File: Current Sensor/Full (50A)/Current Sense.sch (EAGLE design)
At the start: 14 parts, among them IC1 INA169

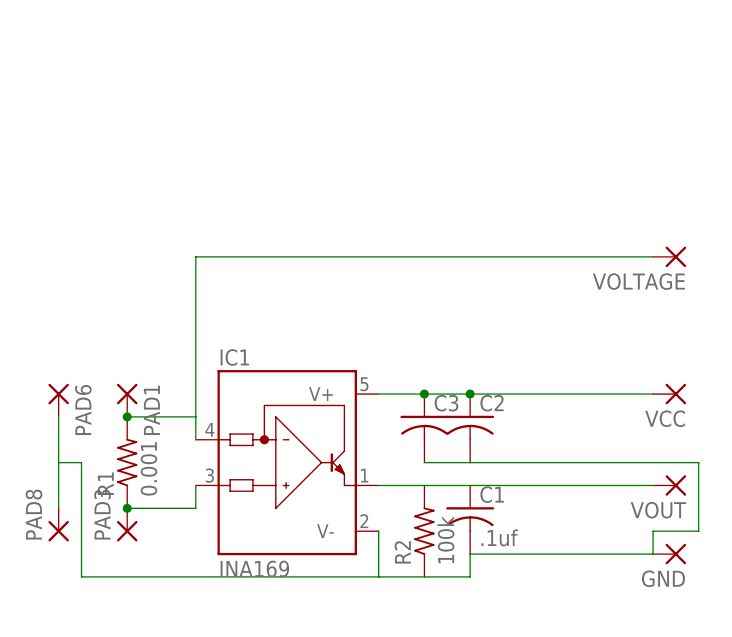
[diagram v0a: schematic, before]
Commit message: Changed Current Sensors
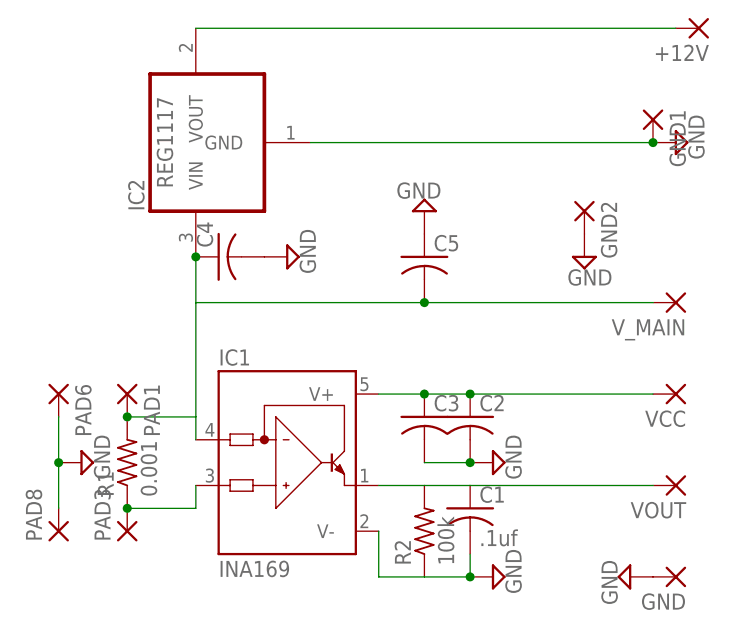
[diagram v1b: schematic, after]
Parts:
- removed VOLTAGE: (no value), wirepad:SMD2
- added +12V, GND1, GND2, V_MAIN: (no value), wirepad:SMD2
- added C4, C5: (no value), adafruit:C-USC0805K
- added IC2: REG1117, burr-brown:REG1117
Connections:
- net N$6 renamed VCC
- removed net N$4: C1.2, C2.2, C3.2, GND.P, IC1.V-, PAD6.P, PAD8.P, R2.1
- new net +12V: +12V.P, IC2.VOUT
- new net GND: C1.2, C2.2, C3.2, C4.2, C5.1, GND.P, GND1.P, GND2.P, IC1.V-, IC2.GND, PAD6.P, PAD8.P, R2.1
- net OUT: now also C4.1, C5.2, IC2.VIN, V_MAIN.P; no longer VOLTAGE.P
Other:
- moved on the sheet: GND
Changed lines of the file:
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@@
 <?xml version="1.0" encoding="utf-8"?>
 <!DOCTYPE eagle SYSTEM "eagle.dtd">
-<eagle version="6.2">
+<eagle version="6.3">
 <drawing>
 <settings>
@@
 <part name="C3" library="adafruit" deviceset="C-US" device="C0805K"/>
 <part name="R1" library="adafruit" deviceset="R-US_" device="R2512" value="0.001"/>
-<part name="VOLTAGE" library="wirepad" deviceset="SMD2" device=""/>
+<part name="V_MAIN" library="wirepad" deviceset="SMD2" device=""/>
+<part name="SUPPLY3" library="supply2" deviceset="GND" device=""/>
+<part name="SUPPLY4" library="supply2" deviceset="GND" device=""/>
+<part name="SUPPLY5" library="supply2" deviceset="GND" device=""/>
+<part name="SUPPLY6" library="supply2" deviceset="GND" device=""/>
+<part name="SUPPLY7" library="supply2" deviceset="GND" device=""/>
+<part name="IC2" library="burr-brown" deviceset="REG1117" device=""/>
+<part name="+12V" library="wirepad" deviceset="SMD2" device=""/>
+<part name="GND1" library="wirepad" deviceset="SMD2" device=""/>
+<part name="GND2" library="wirepad" deviceset="SMD2" device=""/>
+<part name="C4" library="adafruit" deviceset="C-US" device="C0805K"/>
+<part name="C5" library="adafruit" deviceset="C-US" device="C0805K"/>
+<part name="SUPPLY1" library="supply2" deviceset="GND" device=""/>
+<part name="SUPPLY2" library="supply2" deviceset="GND" device=""/>
+<part name="SUPPLY8" library="supply2" deviceset="GND" device=""/>
 </parts>
 <sheets>
@@
 <instance part="VCC" gate="1" x="43.18" y="7.62" rot="R180"/>
 <instance part="VOUT" gate="1" x="43.18" y="-2.54" rot="R180"/>
-<instance part="GND" gate="1" x="43.18" y="-10.16" rot="R180"/>
+<instance part="GND" gate="1" x="43.18" y="-12.7" rot="R180"/>
 <instance part="C2" gate="G$1" x="20.32" y="5.08"/>
 <instance part="C3" gate="G$1" x="15.24" y="5.08"/>
 <instance part="R1" gate="G$1" x="-17.78" y="0" rot="R90"/>
-<instance part="VOLTAGE" gate="1" x="43.18" y="22.86" rot="R180"/>
+<instance part="V_MAIN" gate="1" x="43.18" y="17.78" rot="R180"/>
+<instance part="SUPPLY3" gate="GND" x="43.18" y="35.56" rot="R90"/>
+<instance part="SUPPLY4" gate="GND" x="22.86" y="0" rot="R90"/>
+<instance part="SUPPLY5" gate="GND" x="22.86" y="-12.7" rot="R90"/>
+<instance part="SUPPLY6" gate="GND" x="38.1" y="-12.7" rot="R270"/>
+<instance part="SUPPLY7" gate="GND" x="-22.86" y="0" rot="R90"/>
+<instance part="IC2" gate="G$1" x="-10.16" y="35.56" rot="R90"/>
+<instance part="+12V" gate="1" x="45.72" y="48.26" rot="R180"/>
+<instance part="GND1" gate="1" x="40.64" y="38.1" rot="R270"/>
+<instance part="GND2" gate="1" x="33.02" y="27.94" rot="R270"/>
+<instance part="C4" gate="G$1" x="-7.62" y="22.86" rot="R90"/>
+<instance part="C5" gate="G$1" x="15.24" y="22.86"/>
+<instance part="SUPPLY1" gate="GND" x="15.24" y="27.94" rot="R180"/>
+<instance part="SUPPLY2" gate="GND" x="0" y="22.86" rot="R90"/>
+<instance part="SUPPLY8" gate="GND" x="33.02" y="22.86"/>
 </instances>
 <busses>
@@
 <pinref part="R1" gate="G$1" pin="2"/>
 <junction x="-17.78" y="5.08"/>
-<pinref part="VOLTAGE" gate="1" pin="P"/>
-<wire x1="40.64" y1="22.86" x2="-10.16" y2="22.86" width="0.1524" layer="91"/>
-<wire x1="-10.16" y1="22.86" x2="-10.16" y2="5.08" width="0.1524" layer="91"/>
-</segment>
-</net>
-<net name="N$4" class="0">
-<segment>
-<pinref part="IC1" gate="G$1" pin="V-"/>
-<wire x1="10.16" y1="-7.62" x2="10.16" y2="-12.7" width="0.1524" layer="91"/>
-<pinref part="R2" gate="G$1" pin="1"/>
-<wire x1="10.16" y1="-12.7" x2="15.24" y2="-12.7" width="0.1524" layer="91"/>
-<pinref part="C1" gate="G$1" pin="2"/>
-<wire x1="15.24" y1="-12.7" x2="20.32" y2="-12.7" width="0.1524" layer="91"/>
-<wire x1="20.32" y1="-12.7" x2="20.32" y2="-10.16" width="0.1524" layer="91"/>
-<wire x1="20.32" y1="-10.16" x2="40.64" y2="-10.16" width="0.1524" layer="91"/>
-<pinref part="GND" gate="1" pin="P"/>
-<pinref part="C3" gate="G$1" pin="2"/>
-<pinref part="C2" gate="G$1" pin="2"/>
-<wire x1="15.24" y1="0" x2="20.32" y2="0" width="0.1524" layer="91"/>
-<wire x1="20.32" y1="0" x2="45.72" y2="0" width="0.1524" layer="91"/>
-<wire x1="45.72" y1="0" x2="45.72" y2="-7.62" width="0.1524" layer="91"/>
-<wire x1="45.72" y1="-7.62" x2="40.64" y2="-7.62" width="0.1524" layer="91"/>
-<wire x1="40.64" y1="-7.62" x2="40.64" y2="-10.16" width="0.1524" layer="91"/>
-<wire x1="10.16" y1="-12.7" x2="-22.86" y2="-12.7" width="0.1524" layer="91"/>
-<wire x1="-22.86" y1="-12.7" x2="-22.86" y2="0" width="0.1524" layer="91"/>
-<pinref part="PAD8" gate="1" pin="P"/>
-<pinref part="PAD6" gate="1" pin="P"/>
-<wire x1="-25.4" y1="5.08" x2="-25.4" y2="0" width="0.1524" layer="91"/>
-<wire x1="-25.4" y1="0" x2="-25.4" y2="-5.08" width="0.1524" layer="91"/>
-<wire x1="-22.86" y1="0" x2="-25.4" y2="0" width="0.1524" layer="91"/>
-</segment>
-</net>
-<net name="N$6" class="0">
+<pinref part="V_MAIN" gate="1" pin="P"/>
+<wire x1="15.24" y1="17.78" x2="-10.16" y2="17.78" width="0.1524" layer="91"/>
+<wire x1="-10.16" y1="17.78" x2="-10.16" y2="5.08" width="0.1524" layer="91"/>
+<pinref part="IC2" gate="G$1" pin="VIN"/>
+<wire x1="-10.16" y1="22.86" x2="-10.16" y2="17.78" width="0.1524" layer="91"/>
+<pinref part="C4" gate="G$1" pin="1"/>
+<junction x="-10.16" y="22.86"/>
+<pinref part="C5" gate="G$1" pin="2"/>
+<junction x="15.24" y="17.78"/>
+<wire x1="15.24" y1="17.78" x2="40.64" y2="17.78" width="0.1524" layer="91"/>
+</segment>
+</net>
+<net name="VCC" class="0">
 <segment>
 <pinref part="IC1" gate="G$1" pin="V+"/>
@@
 </segment>
 </net>
+<net name="GND" class="0">
+<segment>
+<pinref part="C2" gate="G$1" pin="2"/>
+<pinref part="C3" gate="G$1" pin="2"/>
+<wire x1="15.24" y1="0" x2="20.32" y2="0" width="0.1524" layer="91"/>
+<pinref part="SUPPLY4" gate="GND" pin="GND"/>
+<junction x="20.32" y="0"/>
+</segment>
+<segment>
+<pinref part="C1" gate="G$1" pin="2"/>
+<wire x1="20.32" y1="-12.7" x2="20.32" y2="-10.16" width="0.1524" layer="91"/>
+<pinref part="SUPPLY5" gate="GND" pin="GND"/>
+<junction x="20.32" y="-12.7"/>
+<pinref part="R2" gate="G$1" pin="1"/>
+<pinref part="IC1" gate="G$1" pin="V-"/>
+<wire x1="10.16" y1="-7.62" x2="10.16" y2="-12.7" width="0.1524" layer="91"/>
+<wire x1="10.16" y1="-12.7" x2="15.24" y2="-12.7" width="0.1524" layer="91"/>
+<wire x1="15.24" y1="-12.7" x2="20.32" y2="-12.7" width="0.1524" layer="91"/>
+</segment>
+<segment>
+<pinref part="GND" gate="1" pin="P"/>
+<pinref part="SUPPLY6" gate="GND" pin="GND"/>
+</segment>
+<segment>
+<pinref part="PAD8" gate="1" pin="P"/>
+<pinref part="PAD6" gate="1" pin="P"/>
+<wire x1="-25.4" y1="5.08" x2="-25.4" y2="0" width="0.1524" layer="91"/>
+<pinref part="SUPPLY7" gate="GND" pin="GND"/>
+<wire x1="-25.4" y1="0" x2="-25.4" y2="-5.08" width="0.1524" layer="91"/>
+<junction x="-25.4" y="0"/>
+</segment>
+<segment>
+<pinref part="IC2" gate="G$1" pin="GND"/>
+<pinref part="SUPPLY3" gate="GND" pin="GND"/>
+<wire x1="2.54" y1="35.56" x2="40.64" y2="35.56" width="0.1524" layer="91"/>
+<pinref part="GND1" gate="1" pin="P"/>
+<junction x="40.64" y="35.56"/>
+</segment>
+<segment>
+<pinref part="C5" gate="G$1" pin="1"/>
+<pinref part="SUPPLY1" gate="GND" pin="GND"/>
+</segment>
+<segment>
+<pinref part="C4" gate="G$1" pin="2"/>
+<pinref part="SUPPLY2" gate="GND" pin="GND"/>
+</segment>
+<segment>
+<pinref part="GND2" gate="1" pin="P"/>
+<pinref part="SUPPLY8" gate="GND" pin="GND"/>
+</segment>
+</net>
+<net name="+12V" class="0">
+<segment>
+<pinref part="IC2" gate="G$1" pin="VOUT"/>
+<wire x1="43.18" y1="48.26" x2="-10.16" y2="48.26" width="0.1524" layer="91"/>
+<pinref part="+12V" gate="1" pin="P"/>
+</segment>
+</net>

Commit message: Updated to V4.0
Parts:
- renumbered PAD1 to OUT, PAD3 to IN
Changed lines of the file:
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@@
 <part name="C1" library="adafruit" deviceset="C-US" device="C0805K" value=".1uf"/>
 <part name="R2" library="adafruit" deviceset="R-US_" device="R0805" value="100k"/>
-<part name="PAD1" library="wirepad" deviceset="SMD5" device=""/>
-<part name="PAD3" library="wirepad" deviceset="SMD5" device=""/>
+<part name="OUT" library="wirepad" deviceset="SMD5" device=""/>
+<part name="IN" library="wirepad" deviceset="SMD5" device=""/>
 <part name="PAD6" library="wirepad" deviceset="SMD5" device=""/>
 <part name="PAD8" library="wirepad" deviceset="SMD5" device=""/>
@@
 <instance part="C1" gate="G$1" x="20.32" y="-5.08"/>
 <instance part="R2" gate="G$1" x="15.24" y="-7.62" rot="R90"/>
-<instance part="PAD1" gate="1" x="-17.78" y="7.62" rot="R270"/>
-<instance part="PAD3" gate="1" x="-17.78" y="-7.62" rot="R90"/>
+<instance part="OUT" gate="1" x="-17.78" y="7.62" rot="R270"/>
+<instance part="IN" gate="1" x="-17.78" y="-7.62" rot="R90"/>
 <instance part="PAD6" gate="1" x="-25.4" y="7.62" rot="R270"/>
 <instance part="PAD8" gate="1" x="-25.4" y="-7.62" rot="R90"/>
@@
 <wire x1="-17.78" y1="5.08" x2="-10.16" y2="5.08" width="0.1524" layer="91"/>
 <wire x1="-10.16" y1="5.08" x2="-10.16" y2="2.54" width="0.1524" layer="91"/>
-<pinref part="PAD1" gate="1" pin="P"/>
+<pinref part="OUT" gate="1" pin="P"/>
 <pinref part="R1" gate="G$1" pin="2"/>
 <junction x="-17.78" y="5.08"/>
@@
 <segment>
 <pinref part="IC1" gate="G$1" pin="IN+"/>
-<pinref part="PAD3" gate="1" pin="P"/>
+<pinref part="IN" gate="1" pin="P"/>
 <pinref part="R1" gate="G$1" pin="1"/>
 <junction x="-17.78" y="-5.08"/>
